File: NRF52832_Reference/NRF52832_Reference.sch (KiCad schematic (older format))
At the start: 50 parts

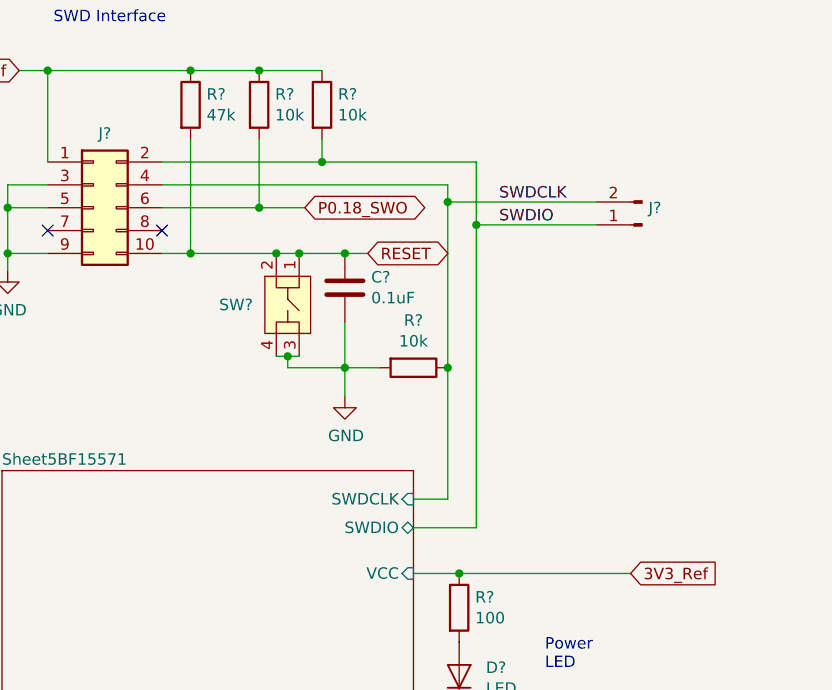
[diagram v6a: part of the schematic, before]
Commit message: Added series resistors for SWDCLK, SWDIO, and SWO
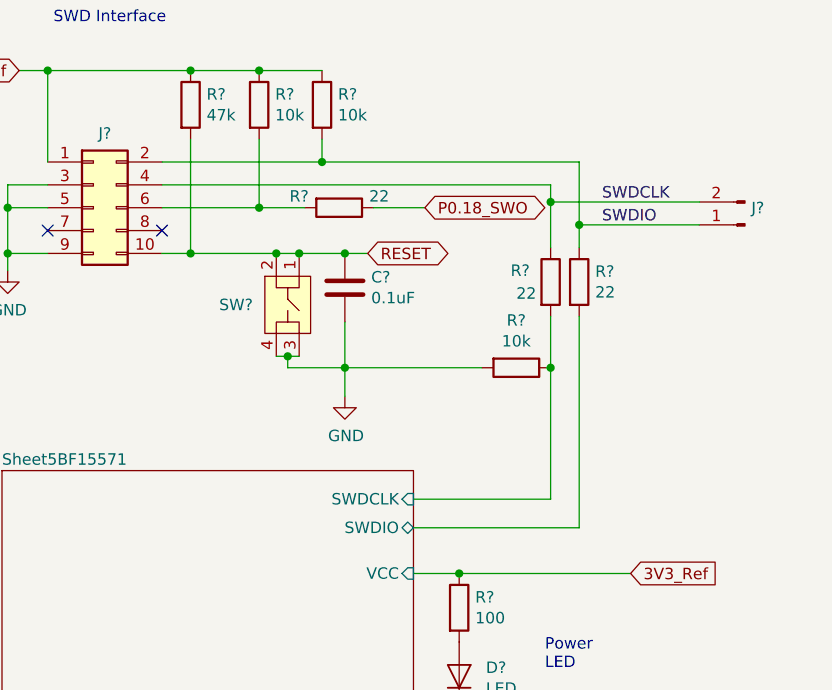
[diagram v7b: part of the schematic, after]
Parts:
- added R? (x3): 22, Resistor_SMD:R_0603_1608Metric_Pad1.05x0.95mm_HandSolder, symbol Device:R
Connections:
- net P0.18_SWO: now also R?.1; no longer J?.6 (Pin_6), R?.2
- net SWDCLK: now also R?.1; no longer R?.1
- net SWDIO: now also R?.1
- new net: J?.6 (Pin_6), R?.2, R?.2
- new net Sheet5BF15571/SWDCLK: R?.1, R?.2
- new net Sheet5BF15571/SWDIO: R?.2
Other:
- moved on the sheet: J?, R?
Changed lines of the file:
@@
 Wire Notes Line
 	475  5425 6950 5425
-Text GLabel 9000 3700 2    50   BiDi ~ 0
+Text GLabel 9525 3700 2    50   BiDi ~ 0
 P0.18_SWO
 Text GLabel 9275 3900 2    50   BiDi ~ 0
@@
 $EndComp
 NoConn ~ 8375 3800
-Wire Wire Line
-	9475 4975 9625 4975
-Wire Wire Line
-	9625 3600 8375 3600
-Wire Wire Line
-	9475 5100 9750 5100
 $Comp
 L Device:R R?
@@
 L Device:R R?
 U 1 1 5C0BEEFE
-P 9475 4400
-F 0 "R?" V 9268 4400 50  0000 C CNN
-F 1 "10k" V 9359 4400 50  0000 C CNN
-F 2 "Resistor_SMD:R_0603_1608Metric_Pad1.05x0.95mm_HandSolder" V 9405 4400 50  0001 C CNN
-F 3 "~" H 9475 4400 50  0001 C CNN
-	1    9475 4400
+P 9925 4400
+F 0 "R?" V 9718 4400 50  0000 C CNN
+F 1 "10k" V 9809 4400 50  0000 C CNN
+F 2 "Resistor_SMD:R_0603_1608Metric_Pad1.05x0.95mm_HandSolder" V 9855 4400 50  0001 C CNN
+F 3 "~" H 9925 4400 50  0001 C CNN
+	1    9925 4400
 	0    1    1    0
 $EndComp
 NoConn ~ 7875 3800
-Wire Wire Line
-	9325 4400 9175 4400
 Wire Wire Line
 	8800 3700 8800 3400
@@
 Wire Wire Line
 	7875 3100 8500 3100
-Connection ~ 9075 3500
-Wire Wire Line
-	9075 3500 9750 3500
 Wire Wire Line
 	8500 3400 8500 3900
@@
 Wire Wire Line
 	9600 2125 9600 2200
-Wire Wire Line
-	9625 4975 9625 4400
-Wire Wire Line
-	9750 5100 9750 3775
 Wire Notes Line
 	475  2575 11225 2575
@@
 L Connector:Conn_01x02_Male J?
 U 1 1 5C377AB0
-P 10475 3775
-F 0 "J?" H 10447 3701 50  0000 R CNN
-F 1 "Conn_01x02_Male" H 10448 3746 50  0001 R CNN
-F 2 "Connector_PinHeader_2.54mm:PinHeader_1x02_P2.54mm_Vertical" H 10475 3775 50  0001 C CNN
-F 3 "~" H 10475 3775 50  0001 C CNN
-	1    10475 3775
+P 10925 3775
+F 0 "J?" H 10897 3701 50  0000 R CNN
+F 1 "Conn_01x02_Male" H 10898 3746 50  0001 R CNN
+F 2 "Connector_PinHeader_2.54mm:PinHeader_1x02_P2.54mm_Vertical" H 10925 3775 50  0001 C CNN
+F 3 "~" H 10925 3775 50  0001 C CNN
+	1    10925 3775
 	-1   0    0    1
 $EndComp
 Wire Wire Line
-	10275 3675 9625 3675
-Connection ~ 9625 3675
-Wire Wire Line
-	9625 3675 9625 3600
-Wire Wire Line
-	10275 3775 9750 3775
-Connection ~ 9750 3775
-Wire Wire Line
-	9750 3775 9750 3500
-Text Label 9850 3675 0    50   ~ 0
+	10725 3675 10075 3675
+Wire Wire Line
+	10075 3675 10075 3600
+Wire Wire Line
+	10725 3775 10200 3775
+Wire Wire Line
+	10200 3775 10200 3500
+Text Label 10300 3675 0    50   ~ 0
 SWDCLK
-Text Label 9850 3775 0    50   ~ 0
+Text Label 10300 3775 0    50   ~ 0
 SWDIO
 Connection ~ 4000 3075
@@
 Wire Wire Line
 	4000 3750 4600 3750
-Connection ~ 9625 4400
-Wire Wire Line
-	9625 3675 9625 4400
 Wire Wire Line
 	9175 4200 9175 4400
@@
 Connection ~ 8975 3900
 Connection ~ 8875 3900
+$Comp
+L Device:R R?
+U 1 1 5C1BC35E
+P 10075 4025
+F 0 "R?" H 9900 4075 50  0000 L CNN
+F 1 "22" H 9925 3975 50  0000 L CNN
+F 2 "Resistor_SMD:R_0603_1608Metric_Pad1.05x0.95mm_HandSolder" V 10005 4025 50  0001 C CNN
+F 3 "~" H 10075 4025 50  0001 C CNN
+	1    10075 4025
+	1    0    0    -1
+$EndComp
+$Comp
+L Device:R R?
+U 1 1 5C1BC400
+P 10200 4025
+F 0 "R?" H 10270 4071 50  0000 L CNN
+F 1 "22" H 10270 3980 50  0000 L CNN
+F 2 "Resistor_SMD:R_0603_1608Metric_Pad1.05x0.95mm_HandSolder" V 10130 4025 50  0001 C CNN
+F 3 "~" H 10200 4025 50  0001 C CNN
+	1    10200 4025
+	1    0    0    -1
+$EndComp
+$Comp
+L Device:R R?
+U 1 1 5C1F2B3E
+P 9150 3700
+F 0 "R?" V 9100 3525 50  0000 C CNN
+F 1 "22" V 9100 3875 50  0000 C CNN
+F 2 "Resistor_SMD:R_0603_1608Metric_Pad1.05x0.95mm_HandSolder" V 9080 3700 50  0001 C CNN
+F 3 "~" H 9150 3700 50  0001 C CNN
+	1    9150 3700
+	0    1    1    0
+$EndComp
+Wire Wire Line
+	9300 3700 9525 3700
+Wire Wire Line
+	9075 3500 10200 3500
+Connection ~ 9075 3500
+Wire Wire Line
+	8375 3600 10075 3600
+Wire Wire Line
+	9475 4975 10075 4975
+Wire Wire Line
+	9475 5100 10200 5100
+Wire Wire Line
+	9175 4400 9775 4400
+Wire Wire Line
+	10075 4400 10075 4975
+Wire Wire Line
+	10075 4400 10075 4175
+Connection ~ 10075 4400
+Wire Wire Line
+	10200 4175 10200 5100
+Wire Wire Line
+	10075 3875 10075 3675
+Connection ~ 10075 3675
+Wire Wire Line
+	10200 3875 10200 3775
+Connection ~ 10200 3775
 $EndSCHEMATC

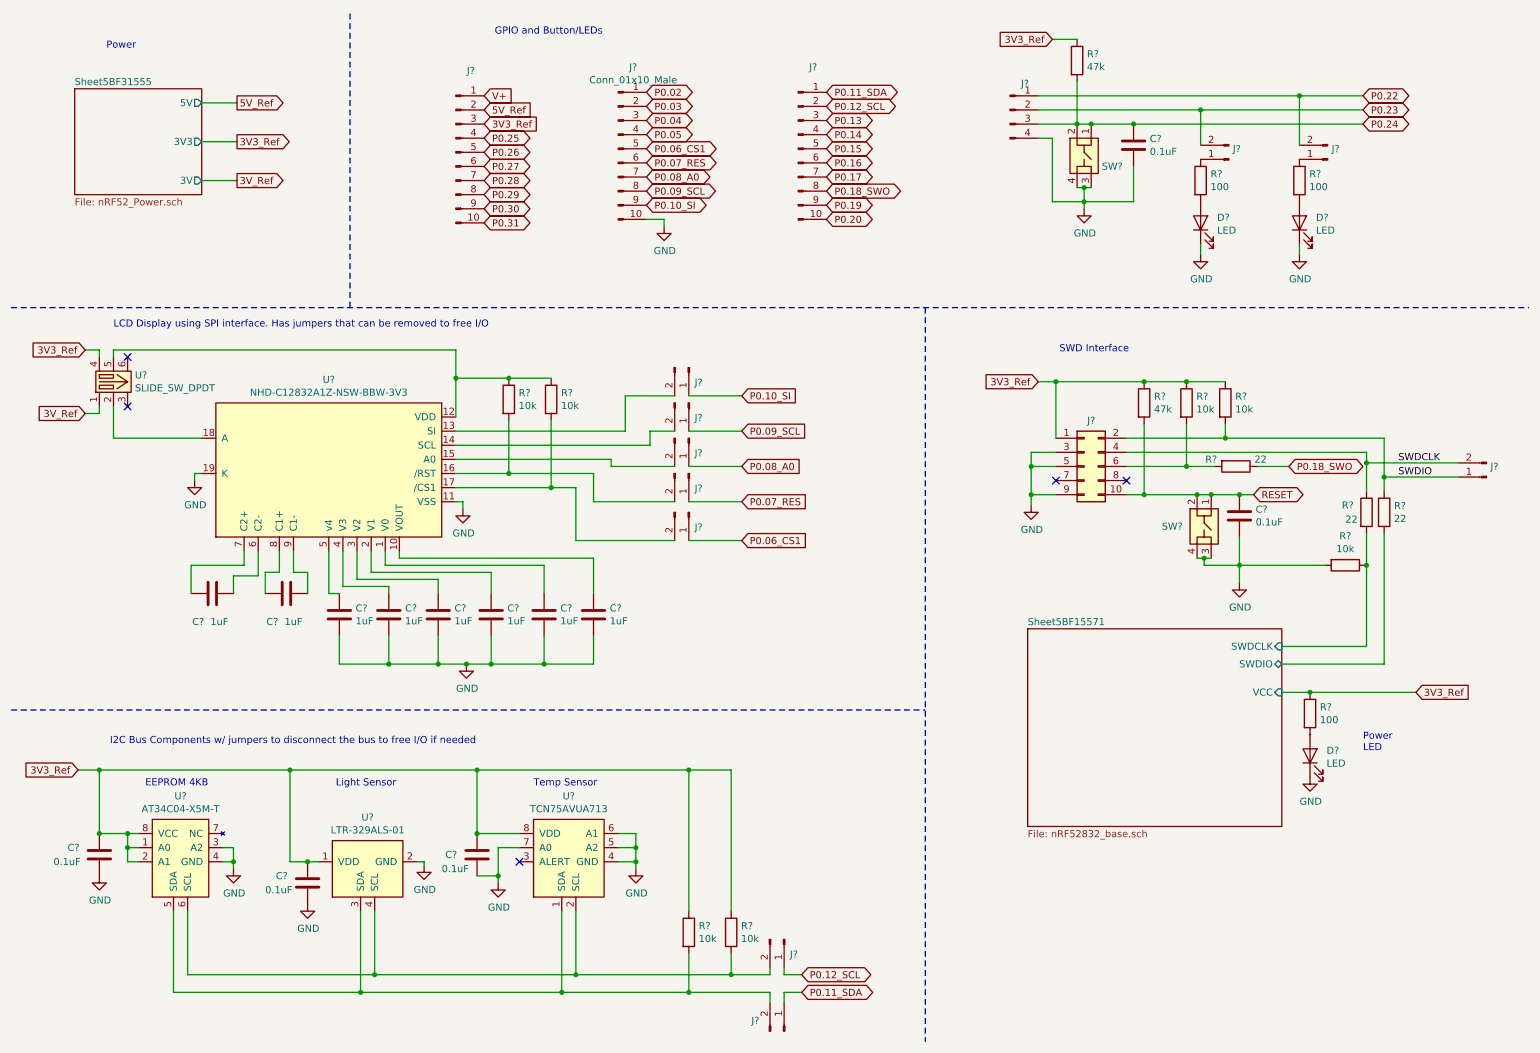
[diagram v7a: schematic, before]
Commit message: Finished footprint assignments for NRF52 base components
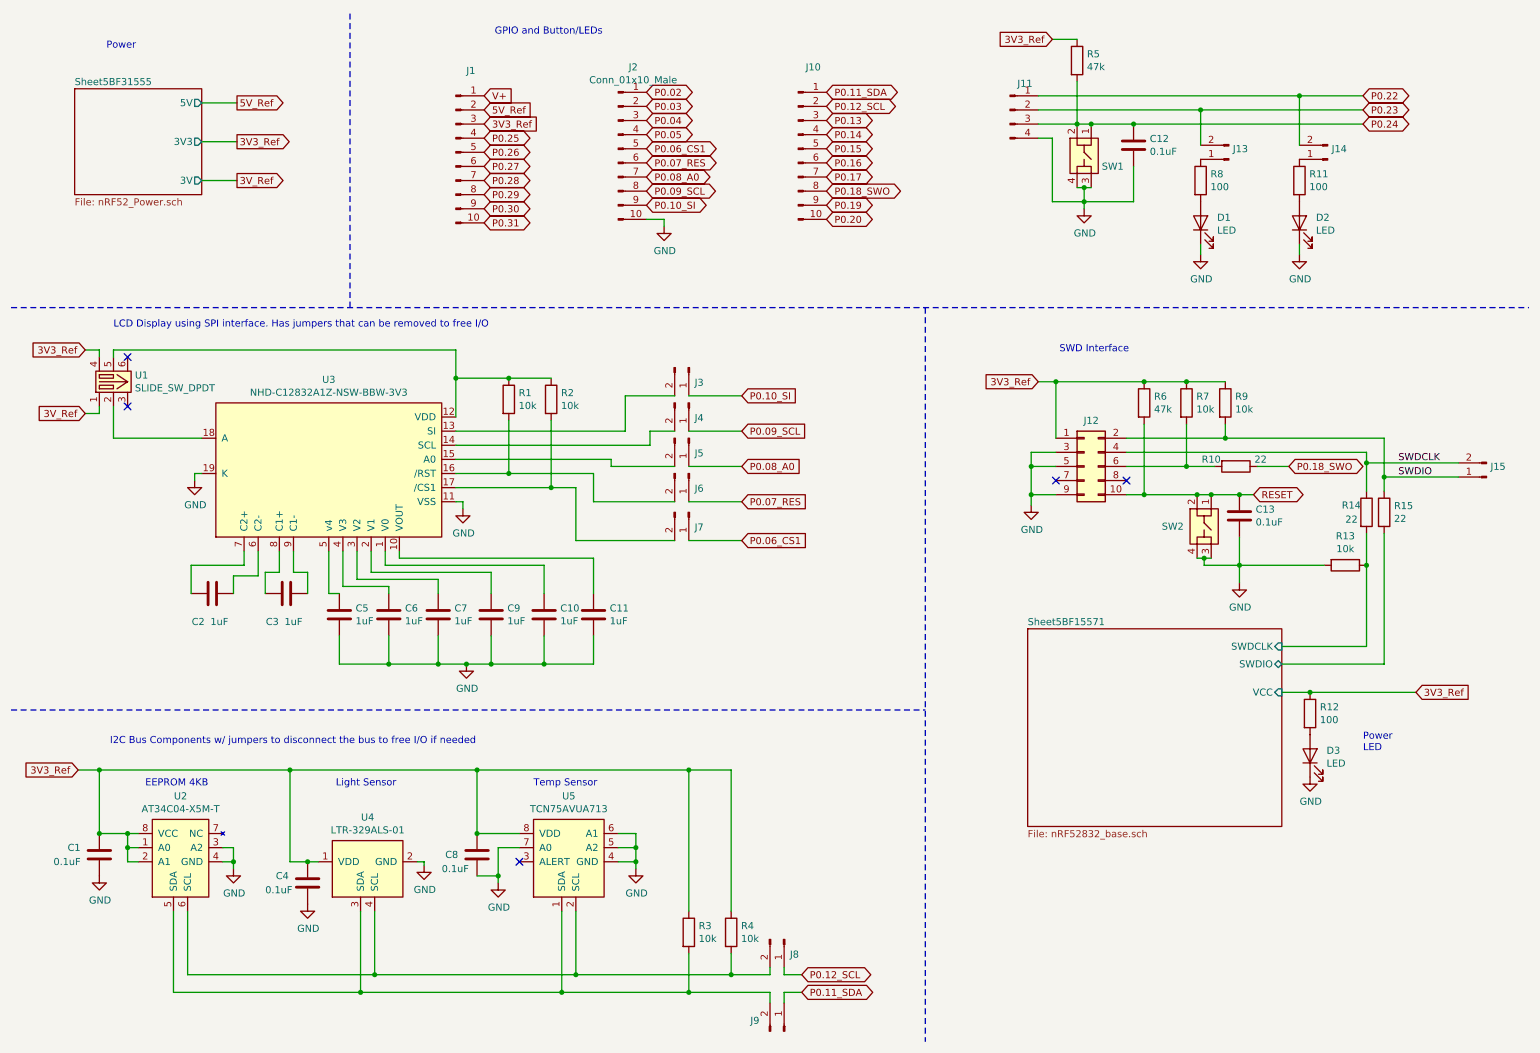
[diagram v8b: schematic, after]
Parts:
- D3: renamed from D?; footprint (none) -> LED_SMD:LED_0603_1608Metric_Pad1.05x0.95mm_HandSolder
- R12: renamed from R?; footprint (none) -> Resistor_SMD:R_0603_1608Metric_Pad1.05x0.95mm_HandSolder
- gave numbers to parts that had none: 51
